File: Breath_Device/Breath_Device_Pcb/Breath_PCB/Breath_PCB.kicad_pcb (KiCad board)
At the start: 2 copper layers, 47.7 x 47.7 mm, 16 parts, among them J1 Conn_01x01_Male, J2 Conn_01x02_Female, J3 Conn_01x01_Male, J4 Conn_01x01_Male, Q1 BUK9M28-80EX, U1 ATtiny85-20PU

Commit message: Stls and Processing Code
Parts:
- moved R7 2.10 mm to (133.2, 79.4), turned to 260 degrees
- moved R8 1.97 mm to (166.3, 94.7)
- moved R5 1.60 mm to (138.1, 85.3)
- moved R4 0.69 mm to (132.7, 101.4), turned to 125 degrees
- moved R2 0.57 mm to (166.6, 98.6), turned to 240 degrees
- moved R1 0.51 mm to (147.4, 65.9)
- moved U1 0.51 mm to (145.4, 69.1)
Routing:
- net +5V: track 109.9 -> 102.8 mm
- net Net-(R1-Pad2): track 108.8 -> 114.3 mm
- net Net-(J4-Pad1): track 31.7 -> 29.7 mm
- net Net-(R5-Pad2): track 10.5 -> 8.95 mm
- net Net-(Q1-Pad5): track 8.16 -> 6.66 mm
- net Net-(R8-Pad2): track 30.7 -> 29.2 mm
- net Net-(D1-Pad2): track 18.9 -> 17.8 mm
- added copper zone on F.Cu, net (none)
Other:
- net class 0.35 added: clearance 0.2, trace_width 0.35, via_dia 0.8, via_drill 0.4

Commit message: more stl files
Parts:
- removed J1, J3: Conn_01x01_Male, Connector_Pin:Pin_D1.3mm_L11.0mm
- U1: moved to B.Cu
- moved U1 7.32 mm to (152.7, 69.6), turned to 180 degrees
- moved J4 4.76 mm to (141.6, 101.6)
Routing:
- net Net-(R1-Pad2): track 114.3 -> 134.0 mm
- net +5V: track 102.8 -> 86.4 mm
- net Net-(R5-Pad2): track 8.95 -> 23.6 mm
- net Net-(R8-Pad2): track 29.2 -> 40.4 mm
- net Net-(J4-Pad1): track 29.7 -> 27.7 mm
- added copper zone on F.Cu, net +5V
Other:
- net class 0.35: clearance 0.2 -> 0.4

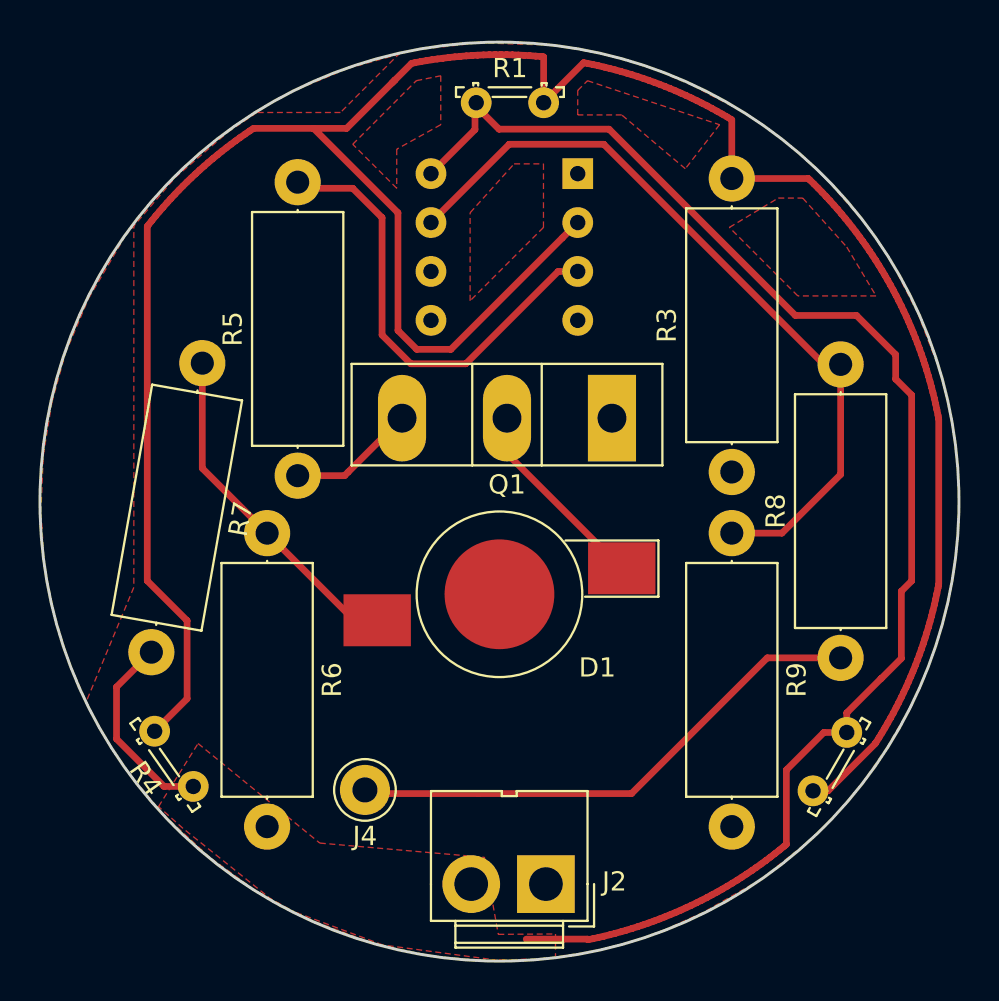
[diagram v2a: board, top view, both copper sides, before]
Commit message: new pcb design and filtered stl files
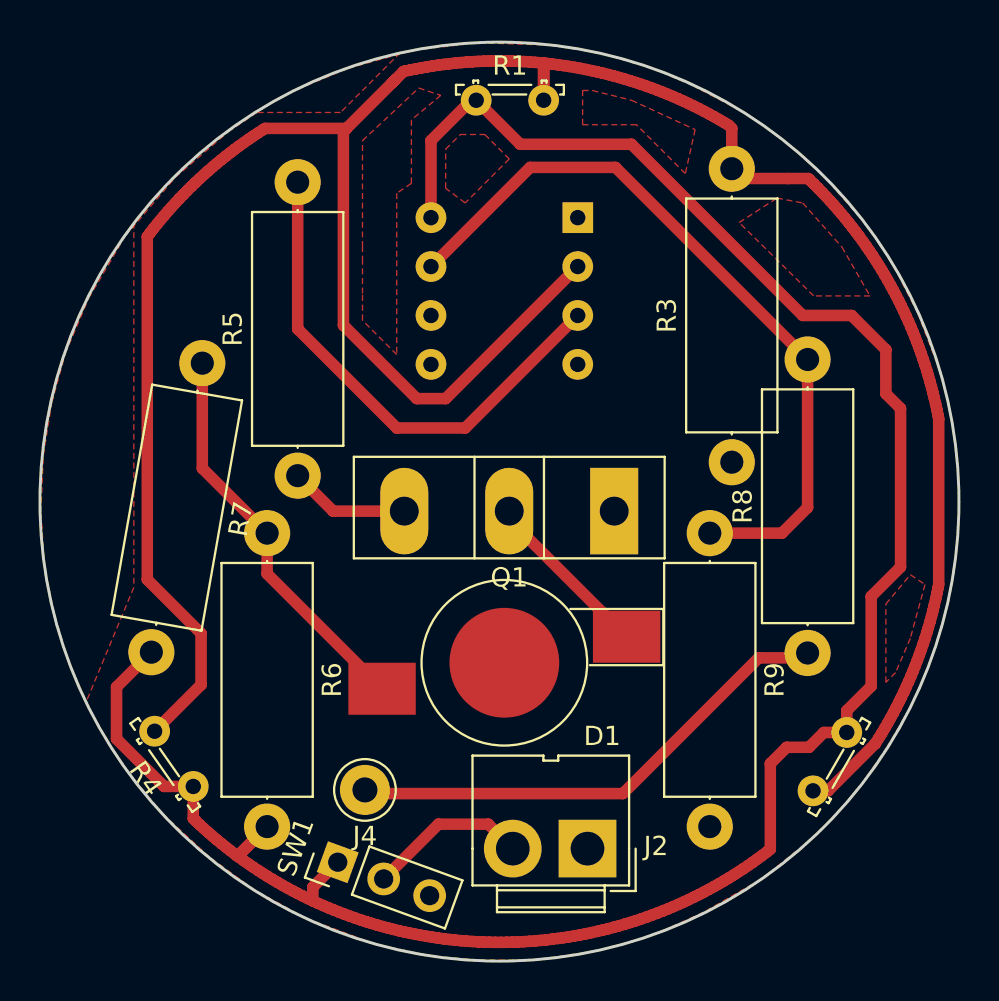
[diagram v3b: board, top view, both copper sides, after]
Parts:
- added SW1: SW_SPDT, Connector_PinHeader_2.54mm:PinHeader_1x03_P2.54mm_Vertical, F.Cu at (140.2, 105.4)
- moved Q1 4.83 mm to (154.5, 87.1)
- moved D1 3.57 mm to (148.8, 95.0)
- moved J2 2.84 mm to (153.2, 104.6)
- moved U1 2.29 mm to (152.7, 71.9)
- moved R8 1.73 mm to (164.6, 94.5)
- moved R9 1.14 mm to (159.5, 88.3)
- moved R3 0.51 mm to (160.7, 84.6)
- moved R1 0.13 mm to (147.4, 65.8)
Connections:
- J2 pad 2: +5V -> Net-(J2-Pad2)
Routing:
- net +5V: track 86.4 -> 116.6 mm
- net Net-(J2-Pad2): track 0.00 -> 8.41 mm
- net Net-(R5-Pad2): track 23.6 -> 26.7 mm
- net Net-(D1-Pad2): track 17.8 -> 20.8 mm
- net Net-(R8-Pad2): track 40.4 -> 38.0 mm
- net Net-(J4-Pad1): track 27.7 -> 26.1 mm
- net Net-(D1-Pad1): track 10.3 -> 9.05 mm
- net Net-(R1-Pad2): track 134.0 -> 134.6 mm
- removed copper zone on F.Cu, net +5V
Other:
- net class 0.35 removed
- net class Regular added: clearance 0.6, trace_width 0.6, via_dia 1.2, via_drill 0.4
